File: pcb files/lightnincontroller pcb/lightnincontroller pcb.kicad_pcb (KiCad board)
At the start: 2 copper layers, 44 parts, among them Q1 BSS138, U1 PIC32MX170F256B-I_SP, U2 TSSOP16-SC16IS740IPW, U3 DS1307N+, Y1 Crystal, Y2 Crystal, Y3 Crystal, con1 icsp

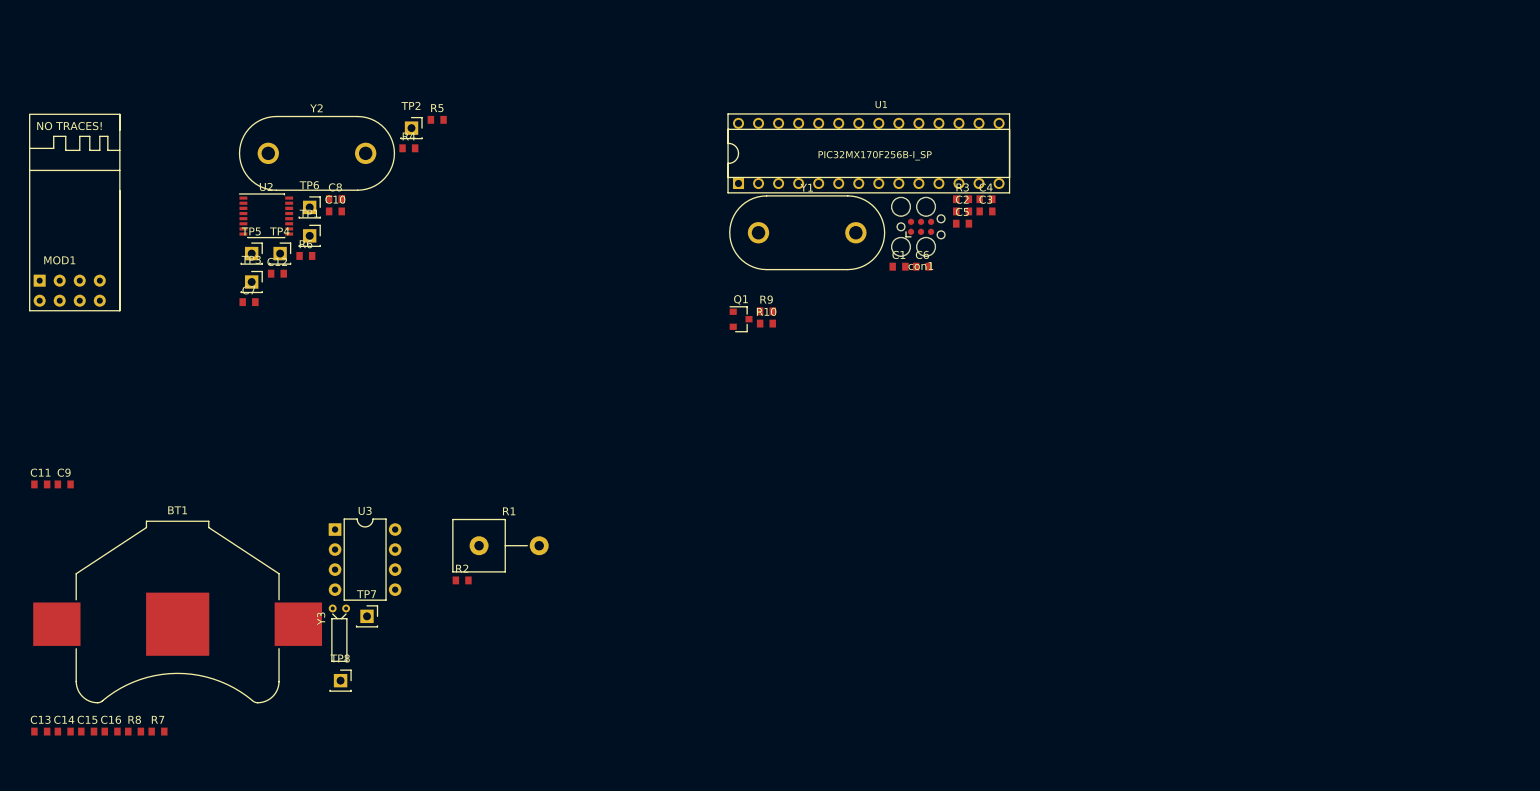
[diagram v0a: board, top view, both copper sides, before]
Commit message: 3de bodys toegevoed
pcb 3d view body;s toegevoegd
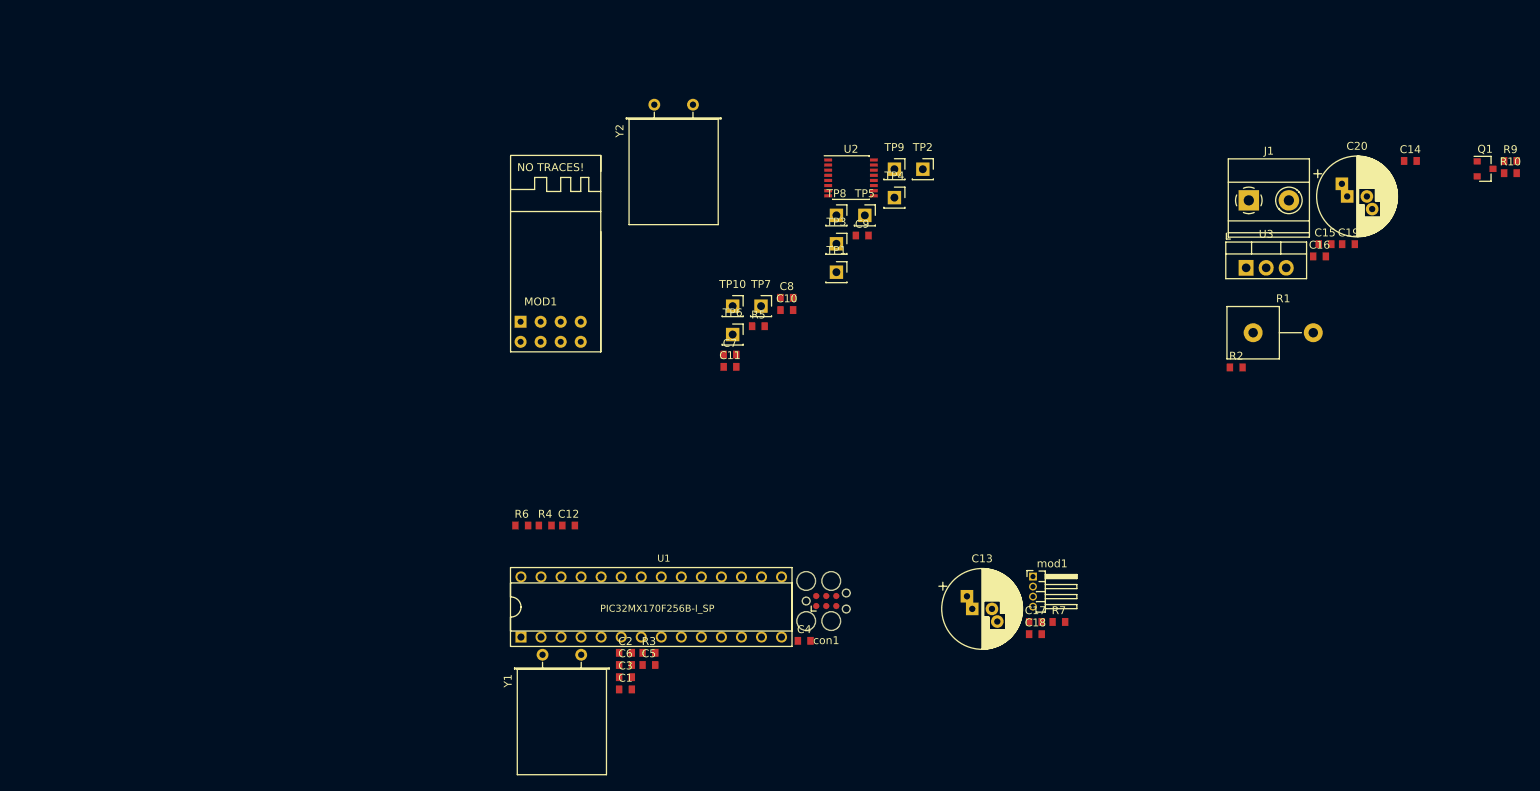
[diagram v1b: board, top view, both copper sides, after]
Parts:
- removed BT1: Battery_Cell, Battery:BatteryHolder_Keystone_3008_1x2450
- removed R8: R, Resistor_SMD:R_0603_1608Metric
- removed Y3: Crystal, Crystal:Crystal_DS15_D1.5mm_L5.0mm_Horizontal
- added C17: C, Capacitor_SMD:C_0603_1608Metric, F.Cu at (151.9, 90.2)
- added C18: C, Capacitor_SMD:C_0603_1608Metric, F.Cu at (151.9, 91.7)
- added C19: C_Small, Capacitor_SMD:C_0603_1608Metric, F.Cu at (191.6, 42.3)
- added C20: C_Small, Capacitor_THT:CP_Radial_D10.0mm_P2.50mm_P5.00mm, F.Cu at (191.4, 36.3)
- added J1: Screw_Terminal_01x02, TerminalBlock_Phoenix:TerminalBlock_Phoenix_MKDS-1,5-2-5.08_1x02_P5.08mm_Horizontal, F.Cu at (179.0, 36.8)
- added TP10: Test_Point, Connector_PinSocket_2.54mm:PinSocket_1x01_P2.54mm_Vertical, F.Cu at (113.6, 50.2)
- added TP9: Test_Point, Connector_PinSocket_2.54mm:PinSocket_1x01_P2.54mm_Vertical, F.Cu at (134.1, 32.8)
- added mod1: Neopixel, Connector_PinHeader_1.27mm:PinHeader_1x04_P1.27mm_Horizontal, F.Cu at (151.6, 84.4)
- C13: value C_Small -> C; footprint Capacitor_SMD:C_0603_1608Metric -> Capacitor_THT:CP_Radial_D10.0mm_P2.50mm_P5.00mm
- U3: value DS1307N+ -> 7833; footprint Package_DIP:DIP-8_W7.62mm -> Package_TO_SOT_THT:TO-220-3_Vertical
- Y1, Y2: footprint Crystal:Crystal_HC33-U_Vertical -> Crystal:Crystal_HC49-U_Horizontal
- moved C14 185.3 mm to (199.4, 31.8)
- moved C15 168.5 mm to (188.6, 42.3)
- moved C16 164.5 mm to (187.9, 43.9)
- moved U3 120.1 mm to (178.6, 45.3)
- moved C13 119.1 mm to (143.9, 88.5)
- moved R7 115.0 mm to (154.9, 90.2)
- moved C9 105.9 mm to (130.0, 41.2)
- moved R1 101.7 mm to (179.5, 53.5)
- moved R2 101.7 mm to (177.4, 57.9)
- moved R10 96.2 mm to (212.1, 33.3)
- moved R9 96.2 mm to (212.1, 31.8)
- moved Q1 96.2 mm to (208.9, 32.8)
- moved C11 88.6 mm to (113.2, 57.9)
- moved TP8 86.2 mm to (126.7, 38.7)
- moved TP4 78.2 mm to (134.1, 36.4)
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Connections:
- net /Sheet5BA79AAB/CH_PD renamed /ESP8266/CH_PD
- net /Sheet5BA79AAB/DISPIRQ renamed Net-(U1-Pad18)
- net /Sheet5BA79AAB/GPIO2 renamed /ESP8266/GPIO2
- net /Sheet5BA79AAB/NEOPIX_OUT1 renamed /controller/NEOPIX_OUT1
- net /Sheet5BA79AAB/PGEC1 renamed /controller/PGEC1
- net /Sheet5BA79AAB/PGED1 renamed /controller/PGED1
- net /Sheet5BA79AAB/PhotoCel renamed /controller/PhotoCel
- net /Sheet5BA79AAB/RESET renamed /ESP8266/RESET
- net /Sheet5BA79AAB/~MCLR renamed /controller/~MCLR
- net /Sheet5BCCFC93/RX renamed /ESP8266/RX
- net /Sheet5BCCFC93/TX renamed /ESP8266/TX
- net /Sheet5BCCFC93/XTAL1 renamed /ESP8266/XTAL1
- net /Sheet5BCCFC93/XTAL2 renamed /ESP8266/XTAL2
- net /Sheet5BCCFC93/~IRQ renamed /ESP8266/~IRQ
- C13 pad 2: +BATT -> VCC
- C14 pad 1: +BATT -> GND
- C14 pad 2: GND -> VCC
- C15 pad 1: Net-(C15-Pad1) -> VCC
- C15 pad 2: +3V3 -> GND
- C16 pad 1: +3V3 -> GND
- C16 pad 2: GND -> +3V3
- MOD1 pad 5: /Sheet5BA79AAB/RST -> /controller/RST
- MOD1 pad 6: /Sheet5BA79AAB/GPIO0 -> /controller/GPIO0
- Q1 pad 3: /Sheet5BD4F2FC/NEOPIX_out -> /Neopixel/DI
- R10 pad 2: /Sheet5BD4F2FC/NEOPIX_out -> /Neopixel/DI
- R5 pad 2: /Sheet5BA79AAB/SCL -> /ESP8266/SCL
- R6 pad 2: /Sheet5BA79AAB/SDA -> /ESP8266/SDA
- R7 pad 1: +3V3 -> /Neopixel/DI
- R7 pad 2: /Sheet5BA79AAB/SCL -> Net-(R7-Pad2)
- TP4 pad 1: /Sheet5BA79AAB/SCL -> /ESP8266/SCL
- TP6 pad 1: /Sheet5BA79AAB/SDA -> /ESP8266/SDA
- TP7 pad 1: /Sheet5BA79AAB/SCL -> /controller/GPIO0
- TP8 pad 1: /Sheet5BA79AAB/SDA -> /controller/RST
- U1 pad 22: /Sheet5BA79AAB/GPIO0 -> /controller/GPIO0
- U1 pad 23: /Sheet5BA79AAB/RST -> /controller/RST
- U1 pad 6: /Sheet5BA79AAB/SDA -> /ESP8266/SDA
- U1 pad 7: /Sheet5BA79AAB/SCL -> /ESP8266/SCL
- U2 pad 5: /Sheet5BA79AAB/SCL -> /ESP8266/SCL
- U2 pad 6: /Sheet5BA79AAB/SDA -> /ESP8266/SDA
- U3 pad 1: Net-(U3-Pad1) -> VCC
- U3 pad 2: Net-(U3-Pad2) -> GND
- U3 pad 3: +BATT -> +3V3

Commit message: pic
pic controller en co gerouted
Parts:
- added D1: 1N4004, Diode_THT:D_DO-41_SOD81_P10.16mm_Horizontal, F.Cu at (59.7, 33.3)
- added D2: 1N4004, Diode_THT:D_DO-41_SOD81_P10.16mm_Horizontal, F.Cu at (53.6, 46.0)
- added J2: Barrel_Jack, Connector_BarrelJack:BarrelJack_Horizontal, F.Cu at (36.6, 33.0)
- R1: footprint Resistor_THT:R_Axial_Power_L20.0mm_W6.4mm_P7.62mm_Vertical -> Resistor_THT:R_Axial_DIN0204_L3.6mm_D1.6mm_P1.90mm_Vertical
- Y1, Y2: footprint Crystal:Crystal_HC49-U_Horizontal -> Crystal:Crystal_HC49-4H_Vertical
- moved R10 181.5 mm to (34.0, 68.3), turned to 90 degrees
- moved R9 175.9 mm to (39.9, 67.6), turned to 90 degrees
- moved Q1 175.3 mm to (37.1, 67.6), turned to 180 degrees
- moved J1 146.1 mm to (33.5, 51.1), turned to 90 degrees
- moved R7 125.2 mm to (31.8, 67.6), turned to 180 degrees
- moved mod1 123.6 mm to (29.0, 69.3), turned to 180 degrees
- moved C20 123.1 mm to (68.3, 36.6), turned to 90 degrees
- moved C14 121.7 mm to (78.0, 39.9), turned to 180 degrees
- moved C17 118.5 mm to (35.1, 70.9)
- moved C18 118.4 mm to (35.1, 72.6), turned to 180 degrees
- moved C15 110.8 mm to (78.0, 37.1)
- moved C19 109.9 mm to (81.7, 40.0), turned to 180 degrees
- moved C13 109.7 mm to (34.5, 79.8), turned to 90 degrees
- moved C16 106.4 mm to (81.8, 37.1)
- moved U3 102.1 mm to (77.2, 33.5)
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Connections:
- J1 pad 2: VCC -> Net-(D2-Pad2)
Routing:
- net VCC: track 0.00 -> 86.7 mm
- net GND: track 0.00 -> 28.8 mm, vias 0 -> 4
- net +3V3: track 0.00 -> 14.1 mm
- net Net-(D1-Pad2): track 0.00 -> 13.1 mm
- net /ESP8266/XTAL1: track 0.00 -> 11.6 mm
- net /ESP8266/XTAL2: track 0.00 -> 11.1 mm
- net Net-(C2-Pad2): track 0.00 -> 10.8 mm
- net Net-(C1-Pad1): track 0.00 -> 9.82 mm
- net /controller/PhotoCel: track 0.00 -> 7.69 mm
- net /Neopixel/DI: track 0.00 -> 3.57 mm
- net Net-(R7-Pad2): track 0.00 -> 2.20 mm
- net /controller/NEOPIX_OUT1: track 0.00 -> 1.86 mm
- added copper zone on B.Cu, net GND
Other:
- board outline added: 96.5 x 58.9 mm
